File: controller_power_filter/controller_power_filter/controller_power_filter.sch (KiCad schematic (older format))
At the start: 22 parts, among them J1 Screw_Terminal_01x03, J2 Screw_Terminal_01x03

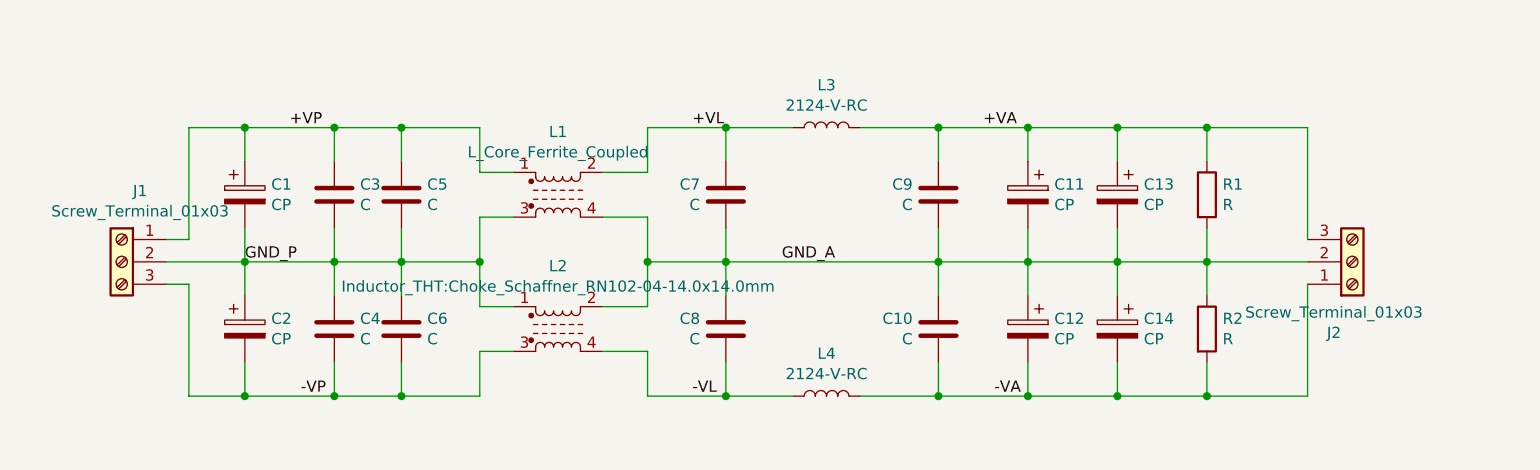
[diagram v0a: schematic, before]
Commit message: minor footprint adjustment to the choke/filter board
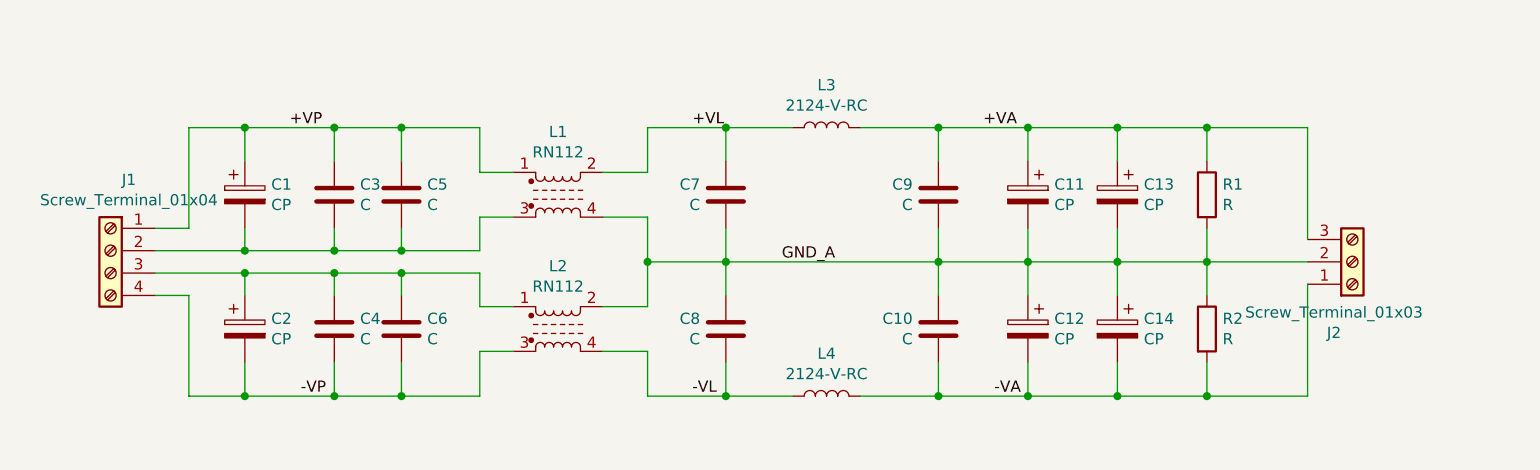
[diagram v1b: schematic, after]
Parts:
- removed J1: Screw_Terminal_01x03, TerminalBlock:TerminalBlock_bornier-3_P5.08mm, symbol Connector:Screw_Terminal_01x03
- added J1: Screw_Terminal_01x04, TerminalBlock:TerminalBlock_bornier-4_P5.08mm, symbol Connector:Screw_Terminal_01x04
- L1: value L_Core_Ferrite_Coupled -> RN112; footprint Inductor_THT:Choke_Schaffner_RN102-04-14.0x14.0mm -> SamacSys_Parts:Choke_Schaffner_RN102_112_204
- L2: value Inductor_THT:Choke_Schaffner_RN102-04-14.0x14.0mm -> RN112; footprint Inductor_THT:Choke_Schaffner_RN102-04-14.0x14.0mm -> SamacSys_Parts:Choke_Schaffner_RN102_112_204
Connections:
- net +VP: now also J1.1 (Pin_1)
- net -VP: now also J1.4 (Pin_4)
- net GND_P: no longer names the net of C1.2, C3.2, C5.2, L1.3
- net GND_P: now also J1.2 (Pin_2); no longer C2.1, C4.1, C6.1, L2.1
- new net: C2.1, C4.1, C6.1, J1.3 (Pin_3), L2.1
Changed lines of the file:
@@
 EESchema Schematic File Version 4
+LIBS:controller_power_filter-cache
 EELAYER 30 0
 EELAYER END
@@
 $EndDescr
 $Comp
-L Device:L_Core_Ferrite_Coupled L1
-U 1 1 614AA517
-P 4550 2850
-F 0 "L1" H 4550 3131 50  0000 C CNN
-F 1 "L_Core_Ferrite_Coupled" H 4550 3040 50  0000 C CNN
-F 2 "Inductor_THT:Choke_Schaffner_RN102-04-14.0x14.0mm" H 4550 2850 50  0001 C CNN
-F 3 "~" H 4550 2850 50  0001 C CNN
-	1    4550 2850
-	1    0    0    -1
-$EndComp
-$Comp
 L Device:C C3
 U 1 1 614AE45E
@@
 P 4550 3450
 F 0 "L2" H 4550 3731 50  0000 C CNN
-F 1 "Inductor_THT:Choke_Schaffner_RN102-04-14.0x14.0mm" H 4550 3640 50  0000 C CNN
-F 2 "Inductor_THT:Choke_Schaffner_RN102-04-14.0x14.0mm" H 4550 3450 50  0001 C CNN
+F 1 "RN112" H 4550 3640 50  0000 C CNN
+F 2 "SamacSys_Parts:Choke_Schaffner_RN102_112_204" H 4550 3450 50  0001 C CNN
 F 3 "~" H 4550 3450 50  0001 C CNN
 	1    4550 3450
@@
 Wire Wire Line
 	4950 3550 4950 3750
-Wire Wire Line
-	3550 3000 3550 3150
-Wire Wire Line
-	3850 3000 3850 3150
 $Comp
 L Device:C C10
@@
 Wire Wire Line
 	7450 3150 7450 3300
-Wire Wire Line
-	3150 3000 3150 3150
-Wire Wire Line
-	4200 2950 4200 3150
-Wire Wire Line
-	3850 3150 4200 3150
-Connection ~ 3850 3150
-Wire Wire Line
-	3850 3150 3850 3300
-Connection ~ 4200 3150
-Wire Wire Line
-	4200 3150 4200 3350
-Wire Wire Line
-	3850 3150 3550 3150
-Connection ~ 3550 3150
-Wire Wire Line
-	3550 3150 3550 3300
-Wire Wire Line
-	3150 3150 3550 3150
-Connection ~ 3150 3150
-Wire Wire Line
-	3150 3150 3150 3300
 Connection ~ 4950 3150
 Wire Wire Line
@@
 	5900 2550 6250 2550
 Connection ~ 6250 2550
-$Comp
-L Connector:Screw_Terminal_01x03 J1
-U 1 1 61516F38
-P 2600 3150
-F 0 "J1" H 2518 3467 50  0000 C CNN
-F 1 "Screw_Terminal_01x03" H 2518 3376 50  0000 C CNN
-F 2 "TerminalBlock:TerminalBlock_bornier-3_P5.08mm" H 2600 3150 50  0001 C CNN
-F 3 "~" H 2600 3150 50  0001 C CNN
-	1    2600 3150
-	-1   0    0    -1
-$EndComp
-Wire Wire Line
-	2800 3150 3150 3150
-Wire Wire Line
-	2800 3050 2900 3050
-Wire Wire Line
-	2900 3050 2900 2550
 Wire Wire Line
 	2900 2550 3150 2550
 Connection ~ 3150 2550
-Wire Wire Line
-	2800 3250 2900 3250
-Wire Wire Line
-	2900 3250 2900 3750
 Wire Wire Line
 	2900 3750 3150 3750
@@
 	7900 2550 7450 2550
 Connection ~ 7450 2550
-Text Label 3150 3150 0    50   ~ 0
-GND_P
 Text Label 5550 3150 0    50   ~ 0
 GND_A
@@
 Text Label 5150 3750 0    50   ~ 0
 -VL
+Wire Wire Line
+	4200 2950 4200 3100
+Wire Wire Line
+	4200 3200 4200 3350
+Wire Wire Line
+	3850 3200 3850 3300
+Connection ~ 3850 3200
+Wire Wire Line
+	3850 3200 4200 3200
+Wire Wire Line
+	3850 3000 3850 3100
+Connection ~ 3850 3100
+Wire Wire Line
+	3850 3100 4200 3100
+Wire Wire Line
+	3150 3000 3150 3100
+Connection ~ 3150 3100
+Wire Wire Line
+	3150 3100 3550 3100
+$Comp
+L Connector:Screw_Terminal_01x04 J1
+U 1 1 6154958E
+P 2550 3100
+F 0 "J1" H 2468 3417 50  0000 C CNN
+F 1 "Screw_Terminal_01x04" H 2468 3326 50  0000 C CNN
+F 2 "TerminalBlock:TerminalBlock_bornier-4_P5.08mm" H 2550 3100 50  0001 C CNN
+F 3 "~" H 2550 3100 50  0001 C CNN
+	1    2550 3100
+	-1   0    0    -1
+$EndComp
+Wire Wire Line
+	2750 3100 3150 3100
+Wire Wire Line
+	2750 3200 3150 3200
+Wire Wire Line
+	3550 3000 3550 3100
+Connection ~ 3550 3100
+Wire Wire Line
+	3550 3100 3850 3100
+Wire Wire Line
+	2750 3300 2900 3300
+Wire Wire Line
+	2900 3300 2900 3750
+Wire Wire Line
+	2750 3000 2900 3000
+Wire Wire Line
+	2900 3000 2900 2550
+Wire Wire Line
+	3550 3300 3550 3200
+Connection ~ 3550 3200
+Wire Wire Line
+	3550 3200 3850 3200
+Wire Wire Line
+	3150 3200 3150 3300
+Connection ~ 3150 3200
+Wire Wire Line
+	3150 3200 3550 3200
+$Comp
+L Device:L_Core_Ferrite_Coupled L1
+U 1 1 614AA517
+P 4550 2850
+F 0 "L1" H 4550 3131 50  0000 C CNN
+F 1 "RN112" H 4550 3040 50  0000 C CNN
+F 2 "SamacSys_Parts:Choke_Schaffner_RN102_112_204" H 4550 2850 50  0001 C CNN
+F 3 "~" H 4550 2850 50  0001 C CNN
+	1    4550 2850
+	1    0    0    -1
+$EndComp
 $EndSCHEMATC

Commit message: Relay array board; Last checkup; Gerberfile updates
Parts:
- removed J2: Screw_Terminal_01x03, TerminalBlock:TerminalBlock_bornier-3_P5.08mm, symbol Connector:Screw_Terminal_01x03
- added J2: Screw_Terminal_01x04, TerminalBlock:TerminalBlock_bornier-4_P5.08mm, symbol Connector:Screw_Terminal_01x04
- added J3, J4: Conn_Coaxial, Connector_Coaxial:U.FL_Hirose_U.FL-R-SMT-1_Vertical, symbol Connector:Conn_Coaxial
- added L5, L6: 2124-V-RC, Inductor_SMD:L_10.4x10.4_H4.8, symbol Device:L
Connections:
- net +VA: now also J2.1 (Pin_1), J3.1 (In), L5.2
- net +VL: now also L5.1
- net -VA: now also J2.4 (Pin_4), J4.1 (In), L6.2
- net -VL: now also L6.1
- net GND_A: no longer names the net of C11.2, C13.2, C7.2, C9.2, L1.4, R1.2
- net GND_A: now also J2.2 (Pin_2), J3.2 (Ext); no longer C10.1, C12.1, C14.1, C8.1, L2.2, R2.1
- new net: C10.1, C12.1, C14.1, C8.1, J2.3 (Pin_3), J4.2 (Ext), L2.2, R2.1
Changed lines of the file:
@@
 	6650 2550 6250 2550
 Wire Wire Line
-	6250 3150 6250 3000
-Wire Wire Line
-	6650 3000 6650 3150
-Wire Wire Line
-	6650 3150 6250 3150
-Connection ~ 6250 3150
-Wire Wire Line
 	6250 2700 6250 2550
-Wire Wire Line
-	5300 2700 5300 2550
-Wire Wire Line
-	5300 2550 4950 2550
 Wire Wire Line
 	4950 2550 4950 2750
@@
 	7050 2700 7050 2550
 Wire Wire Line
-	7050 3000 7050 3150
-Wire Wire Line
-	7050 3150 6650 3150
-Connection ~ 6650 3150
-Wire Wire Line
 	7050 2550 6650 2550
 Connection ~ 6650 2550
@@
 $EndComp
 Wire Wire Line
-	7450 3000 7450 3150
-Wire Wire Line
-	7450 3150 7050 3150
-Connection ~ 7050 3150
-Wire Wire Line
 	7050 2550 7450 2550
 Wire Wire Line
@@
 	3850 3750 3550 3750
 Wire Wire Line
-	4950 3750 5300 3750
-Wire Wire Line
-	5300 3600 5300 3750
-Wire Wire Line
 	4950 3350 4750 3350
 Wire Wire Line
@@
 $EndComp
 Wire Wire Line
-	6650 3300 6650 3150
-Wire Wire Line
 	6250 3750 6250 3600
 Wire Wire Line
@@
 Wire Wire Line
 	6650 3750 6250 3750
-Wire Wire Line
-	6250 3300 6250 3150
 $Comp
 L Device:CP C14
@@
 $EndComp
 Wire Wire Line
-	7050 3300 7050 3150
-Wire Wire Line
 	7050 3600 7050 3750
 Wire Wire Line
@@
 	7450 3750 7050 3750
 Connection ~ 7050 3750
-Wire Wire Line
-	7450 3150 7450 3300
-Connection ~ 4950 3150
-Wire Wire Line
-	4950 2950 4950 3150
-Wire Wire Line
-	4950 3150 4950 3350
-Wire Wire Line
-	4950 3150 5300 3150
-Connection ~ 5300 3150
-Wire Wire Line
-	5300 3300 5300 3150
-$Comp
-L Device:C C8
-U 1 1 614CA44D
-P 5300 3450
-F 0 "C8" H 5415 3496 50  0000 L CNN
-F 1 "C" H 5415 3405 50  0000 L CNN
-F 2 "SamacSys_Parts:C_1206_0805_dual" H 5338 3300 50  0001 C CNN
-F 3 "~" H 5300 3450 50  0001 C CNN
-	1    5300 3450
-	-1   0    0    -1
-$EndComp
-Wire Wire Line
-	5300 3000 5300 3150
-$Comp
-L Device:C C7
-U 1 1 614B651F
-P 5300 2850
-F 0 "C7" H 5415 2896 50  0000 L CNN
-F 1 "C" H 5415 2805 50  0000 L CNN
-F 2 "SamacSys_Parts:C_1206_0805_dual" H 5338 2700 50  0001 C CNN
-F 3 "~" H 5300 2850 50  0001 C CNN
-	1    5300 2850
-	-1   0    0    -1
-$EndComp
-Wire Wire Line
-	5300 3150 6250 3150
 $Comp
 L Device:L L3
@@
 Connection ~ 6250 3750
 Wire Wire Line
-	5600 3750 5300 3750
-Connection ~ 5300 3750
-Wire Wire Line
-	5600 2550 5300 2550
-Connection ~ 5300 2550
-Wire Wire Line
 	5900 2550 6250 2550
 Connection ~ 6250 2550
@@
 	2900 3750 3150 3750
 Connection ~ 3150 3750
-$Comp
-L Connector:Screw_Terminal_01x03 J2
-U 1 1 6151EC1A
-P 8100 3150
-F 0 "J2" H 8018 3467 50  0000 C CNN
-F 1 "Screw_Terminal_01x03" H 8018 3376 50  0000 C CNN
-F 2 "TerminalBlock:TerminalBlock_bornier-3_P5.08mm" H 8100 3150 50  0001 C CNN
-F 3 "~" H 8100 3150 50  0001 C CNN
-	1    8100 3150
-	1    0    0    1
-$EndComp
-Wire Wire Line
-	7900 3150 7450 3150
-Connection ~ 7450 3150
-Wire Wire Line
-	7900 3250 7900 3750
 Wire Wire Line
 	7900 3750 7450 3750
 Connection ~ 7450 3750
 Wire Wire Line
-	7900 3050 7900 2550
-Wire Wire Line
 	7900 2550 7450 2550
 Connection ~ 7450 2550
-Text Label 5550 3150 0    50   ~ 0
-GND_A
 Text Label 6450 2550 0    50   ~ 0
 +VA
@@
 	1    0    0    -1
 $EndComp
+$Comp
+L Connector:Screw_Terminal_01x04 J2
+U 1 1 6135BC8B
+P 8400 3100
+F 0 "J2" H 8318 3417 50  0000 C CNN
+F 1 "Screw_Terminal_01x04" H 8318 3326 50  0000 C CNN
+F 2 "TerminalBlock:TerminalBlock_bornier-4_P5.08mm" H 8400 3100 50  0001 C CNN
+F 3 "~" H 8400 3100 50  0001 C CNN
+	1    8400 3100
+	1    0    0    -1
+$EndComp
+Wire Wire Line
+	4950 3100 4950 2950
+Wire Wire Line
+	5600 3750 5300 3750
+Wire Wire Line
+	4950 3750 5300 3750
+Connection ~ 5300 3750
+Wire Wire Line
+	5300 3600 5300 3750
+$Comp
+L Device:C C8
+U 1 1 614CA44D
+P 5300 3450
+F 0 "C8" H 5415 3496 50  0000 L CNN
+F 1 "C" H 5415 3405 50  0000 L CNN
+F 2 "SamacSys_Parts:C_1206_0805_dual" H 5338 3300 50  0001 C CNN
+F 3 "~" H 5300 3450 50  0001 C CNN
+	1    5300 3450
+	-1   0    0    -1
+$EndComp
+Wire Wire Line
+	5600 2550 5300 2550
+Wire Wire Line
+	5300 2550 4950 2550
+Connection ~ 5300 2550
+Wire Wire Line
+	5300 2700 5300 2550
+Wire Wire Line
+	5300 3000 5300 3100
+Wire Wire Line
+	8200 3100 8150 3100
+Wire Wire Line
+	5300 3100 4950 3100
+Connection ~ 5300 3100
+$Comp
+L Device:C C7
+U 1 1 614B651F
+P 5300 2850
+F 0 "C7" H 5415 2896 50  0000 L CNN
+F 1 "C" H 5415 2805 50  0000 L CNN
+F 2 "SamacSys_Parts:C_1206_0805_dual" H 5338 2700 50  0001 C CNN
+F 3 "~" H 5300 2850 50  0001 C CNN
+	1    5300 2850
+	-1   0    0    -1
+$EndComp
+Wire Wire Line
+	4950 3350 4950 3200
+Wire Wire Line
+	4950 3200 5300 3200
+Wire Wire Line
+	5300 3300 5300 3200
+Connection ~ 5300 3200
+Wire Wire Line
+	5300 3200 6250 3200
+Wire Wire Line
+	6250 3000 6250 3100
+Connection ~ 6250 3100
+Wire Wire Line
+	6250 3100 5300 3100
+Wire Wire Line
+	6250 3300 6250 3200
+Connection ~ 6250 3200
+Wire Wire Line
+	6250 3200 6650 3200
+Wire Wire Line
+	6650 3300 6650 3200
+Connection ~ 6650 3200
+Wire Wire Line
+	6650 3200 7050 3200
+Wire Wire Line
+	6650 3100 6650 3000
+Connection ~ 6650 3100
+Wire Wire Line
+	6650 3100 6250 3100
+Wire Wire Line
+	7050 3000 7050 3100
+Connection ~ 7050 3100
+Wire Wire Line
+	7050 3100 6650 3100
+Wire Wire Line
+	7050 3200 7050 3300
+Connection ~ 7050 3200
+Wire Wire Line
+	7050 3200 7450 3200
+Wire Wire Line
+	7450 3300 7450 3200
+Connection ~ 7450 3200
+Wire Wire Line
+	7450 3200 8150 3200
+Wire Wire Line
+	7450 3000 7450 3100
+Connection ~ 7450 3100
+Wire Wire Line
+	7450 3100 7050 3100
+Wire Wire Line
+	8200 3000 7900 3000
+Wire Wire Line
+	7900 3000 7900 2550
+Wire Wire Line
+	8200 3300 7900 3300
+Wire Wire Line
+	7900 3300 7900 3750
+$Comp
+L Connector:Conn_Coaxial J3
+U 1 1 613A2745
+P 8150 2550
+F 0 "J3" H 8250 2525 50  0000 L CNN
+F 1 "Conn_Coaxial" H 8250 2434 50  0000 L CNN
+F 2 "Connector_Coaxial:U.FL_Hirose_U.FL-R-SMT-1_Vertical" H 8150 2550 50  0001 C CNN
+F 3 " ~" H 8150 2550 50  0001 C CNN
+	1    8150 2550
+	1    0    0    -1
+$EndComp
+Wire Wire Line
+	8150 2750 8150 3100
+Connection ~ 8150 3100
+Wire Wire Line
+	8150 3100 7450 3100
+Wire Wire Line
+	7950 2550 7900 2550
+Connection ~ 7900 2550
+$Comp
+L Connector:Conn_Coaxial J4
+U 1 1 613A8E32
+P 8150 3750
+F 0 "J4" H 8250 3725 50  0000 L CNN
+F 1 "Conn_Coaxial" H 8250 3634 50  0000 L CNN
+F 2 "Connector_Coaxial:U.FL_Hirose_U.FL-R-SMT-1_Vertical" H 8150 3750 50  0001 C CNN
+F 3 " ~" H 8150 3750 50  0001 C CNN
+	1    8150 3750
+	1    0    0    1
+$EndComp
+Wire Wire Line
+	8150 3550 8150 3200
+Connection ~ 8150 3200
+Wire Wire Line
+	8150 3200 8200 3200
+Wire Wire Line
+	7950 3750 7900 3750
+Connection ~ 7900 3750
+$Comp
+L Device:L L5
+U 1 1 613B7AF5
+P 5750 2300
+F 0 "L5" V 5940 2300 50  0000 C CNN
+F 1 "2124-V-RC" V 5849 2300 50  0000 C CNN
+F 2 "Inductor_SMD:L_10.4x10.4_H4.8" H 5750 2300 50  0001 C CNN
+F 3 "~" H 5750 2300 50  0001 C CNN
+	1    5750 2300
+	0    -1   -1   0
+$EndComp
+Wire Wire Line
+	5900 2300 6250 2300
+Wire Wire Line
+	6250 2300 6250 2550
+Wire Wire Line
+	5600 2300 5300 2300
+Wire Wire Line
+	5300 2300 5300 2550
+$Comp
+L Device:L L6
+U 1 1 613C18D1
+P 5750 4000
+F 0 "L6" V 5940 4000 50  0000 C CNN
+F 1 "2124-V-RC" V 5849 4000 50  0000 C CNN
+F 2 "Inductor_SMD:L_10.4x10.4_H4.8" H 5750 4000 50  0001 C CNN
+F 3 "~" H 5750 4000 50  0001 C CNN
+	1    5750 4000
+	0    -1   -1   0
+$EndComp
+Wire Wire Line
+	5900 4000 6250 4000
+Wire Wire Line
+	6250 4000 6250 3750
+Wire Wire Line
+	5300 3750 5300 4000
+Wire Wire Line
+	5300 4000 5600 4000
 $EndSCHEMATC
